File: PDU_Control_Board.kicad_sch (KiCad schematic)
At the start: 151 parts, among them J1 24V, J10 Precharge_2, J11 Shunt_2, J12 VIN_Enable, J13 VDC_IN_P, J14 VDC_IN_N, J15 VDC_OUT1_P, J16 VDC_OUT1_N, J17 VDC_OUT2_P, J18 VDC_OUT2_N, J19 24V, J2 Shunt_1, J3 SWD, J4 Precharge_1, J5 Precharge_2, J6 Shunt_2, J7 VIN_Enable, J8 Precharge_1, J9 Shunt_1, Q1 BSP75N, Q2 BSP75N, Q3 BSP75N, Q4 BSP75N, Q5 BSP75N, U1 LMV321, U2 APM32F405xG, U3 LMV321, U4 LMV321, U5 LMV321, Y2 X322516MOB4SI

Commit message: VER1.0: добавил в схему индикацию замыкания
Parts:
- removed J10: Precharge_2, Connector_PinHeader_2.54mm:PinHeader_2x02_P2.54mm_Vertical, symbol Connector_Generic:Conn_02x02_Odd_Even
- removed J11: Shunt_2, Connector_PinHeader_2.54mm:PinHeader_2x02_P2.54mm_Vertical, symbol Connector_Generic:Conn_02x02_Odd_Even
- removed J12: VIN_Enable, Connector_PinHeader_2.54mm:PinHeader_2x02_P2.54mm_Vertical, symbol Connector_Generic:Conn_02x02_Odd_Even
- removed J13: VDC_IN_P, Connector_PinHeader_2.54mm:PinHeader_2x02_P2.54mm_Vertical, symbol Connector_Generic:Conn_02x02_Odd_Even
- removed J14: VDC_IN_N, Connector_PinHeader_2.54mm:PinHeader_2x02_P2.54mm_Vertical, symbol Connector_Generic:Conn_02x02_Odd_Even
- removed J15: VDC_OUT1_P, Connector_PinHeader_2.54mm:PinHeader_2x02_P2.54mm_Vertical, symbol Connector_Generic:Conn_02x02_Odd_Even
- removed J16: VDC_OUT1_N, Connector_PinHeader_2.54mm:PinHeader_2x02_P2.54mm_Vertical, symbol Connector_Generic:Conn_02x02_Odd_Even
- removed J17: VDC_OUT2_P, Connector_PinHeader_2.54mm:PinHeader_2x02_P2.54mm_Vertical, symbol Connector_Generic:Conn_02x02_Odd_Even
- removed J18: VDC_OUT2_N, Connector_PinHeader_2.54mm:PinHeader_2x02_P2.54mm_Vertical, symbol Connector_Generic:Conn_02x02_Odd_Even
- removed J19: 24V, Connector_PinHeader_2.54mm:PinHeader_2x02_P2.54mm_Vertical, symbol Connector_Generic:Conn_02x02_Odd_Even
- removed J8: Precharge_1, Connector_PinHeader_2.54mm:PinHeader_2x02_P2.54mm_Vertical, symbol Connector_Generic:Conn_02x02_Odd_Even
- removed J9: Shunt_1, Connector_PinHeader_2.54mm:PinHeader_2x02_P2.54mm_Vertical, symbol Connector_Generic:Conn_02x02_Odd_Even
- added C39, C40, C41, C42, C43: 2.2u, Capacitor_SMD:C_0805_2012Metric_Pad1.18x1.45mm_HandSolder, symbol Device:C_Small
- added J10: Precharge_2, Connector_Molex:Molex_Mini-Fit_Jr_5569-02A2_2x01_P4.20mm_Horizontal, symbol Connector_Generic:Conn_01x02
- added J11: Shunt_2, Connector_Molex:Molex_Mini-Fit_Jr_5569-02A2_2x01_P4.20mm_Horizontal, symbol Connector_Generic:Conn_01x02
- added J12: VIN_Enable, Connector_Molex:Molex_Mini-Fit_Jr_5569-02A2_2x01_P4.20mm_Horizontal, symbol Connector_Generic:Conn_01x02
- added J20: VDC_OUT2, Connector_Molex:Molex_Mini-Fit_Jr_5569-02A2_2x01_P4.20mm_Horizontal, symbol Connector_Generic:Conn_01x02
- added J21: VDC_OUT1, Connector_Molex:Molex_Mini-Fit_Jr_5569-02A2_2x01_P4.20mm_Horizontal, symbol Connector_Generic:Conn_01x02
- added J22: VDC_IN, Connector_Molex:Molex_Mini-Fit_Jr_5569-02A2_2x01_P4.20mm_Horizontal, symbol Connector_Generic:Conn_01x02
- added J8: Precharge_1, Connector_Molex:Molex_Mini-Fit_Jr_5569-02A2_2x01_P4.20mm_Horizontal, symbol Connector_Generic:Conn_01x02
- added J9: Shunt_1, Connector_Molex:Molex_Mini-Fit_Jr_5569-02A2_2x01_P4.20mm_Horizontal, symbol Connector_Generic:Conn_01x02
- added Q10, Q6, Q7, Q8, Q9: BC817, Package_TO_SOT_SMD:SOT-23, symbol Transistor_BJT:BC817
- added R65, R67, R69, R71, R73: 2.2k, Resistor_SMD:R_0805_2012Metric_Pad1.20x1.40mm_HandSolder, symbol Device:R_Small
- added R66, R68, R70, R72, R74: 1k, Resistor_SMD:R_0805_2012Metric_Pad1.20x1.40mm_HandSolder, symbol Device:R_Small
- C14, C15: footprint Capacitor_SMD:C_0603_1608Metric_Pad1.08x0.95mm_HandSolder -> Capacitor_SMD:C_0805_2012Metric_Pad1.18x1.45mm_HandSolder
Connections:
- net +24V: now also J10.1 (Pin_1), J11.1 (Pin_1), J12.1 (Pin_1), J8.1 (Pin_1), J9.1 (Pin_1)
- net +3.3V: now also R66.2, R68.2, R70.2, R72.2, R74.2
- net GND: now also C39.2, C40.2, C41.2, C42.2, C43.2, Q10.2 (E), Q6.2 (E), Q7.2 (E), Q8.2 (E), Q9.2 (E)
- net VDC_IN_N: now also J22.2 (Pin_2)
- net VDC_IN_P: now also J22.1 (Pin_1)
- net VDC_IN_SENSE: now also U2.30 (PA5)
- net VDC_OUT1_N: now also J21.2 (Pin_2)
- net VDC_OUT1_P: now also J21.1 (Pin_1)
- net VDC_OUT1_SENSE: now also U2.31 (PA6)
- net VDC_OUT2_N: now also J20.2 (Pin_2)
- net VDC_OUT2_P: now also J20.1 (Pin_1)
- net VDC_OUT2_SENSE: now also U2.32 (PA7)
- new net: Q9.1 (B), R71.2
- new net: J12.2 (Pin_2), R73.1
- new net: Q10.1 (B), R73.2
- new net: J10.2 (Pin_2), R69.1
- new net: Q6.1 (B), R65.2
- new net: J9.2 (Pin_2), R67.1
- new net: Q7.1 (B), R67.2
- new net: J8.2 (Pin_2), R65.1
- new net: J11.2 (Pin_2), R71.1
- new net: Q8.1 (B), R69.2
- new net ~{Precharge_1_ON}: C39.1, Q6.3 (C), R66.1
- new net ~{Precharge_2_ON}: C41.1, Q8.3 (C), R70.1
- new net ~{Shunt_1_ON}: C40.1, Q7.3 (C), R68.1
- new net ~{Shunt_2_ON}: C42.1, Q9.3 (C), R72.1
- new net ~{VIN_Enable_ON}: C43.1, Q10.3 (C), R74.1
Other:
- note added: "Индикация замыкания контакторов"
- moved on the sheet: C13, C14, C15, C9, D10, D11, D12, D13, D14, D15, D3, D4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

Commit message: VER1.0: разместил все на плате
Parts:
- removed J1: 24V, Connector_Molex:Molex_Mini-Fit_Jr_5569-02A2_2x01_P4.20mm_Horizontal, symbol Connector_Generic:Conn_01x02
- added C44: 100n, Capacitor_SMD:C_0805_2012Metric_Pad1.18x1.45mm_HandSolder, symbol Device:C
- added C45: 0.27u, Capacitor_SMD:C_0805_2012Metric_Pad1.18x1.45mm_HandSolder, symbol Device:C
- added C46: 56p, Capacitor_SMD:C_0805_2012Metric_Pad1.18x1.45mm_HandSolder, symbol Device:C
- added D19, D20, D21, D22, D23, D24, D25, D26, D27: LED_Small, LED_SMD:LED_0805_2012Metric, symbol Device:LED_Small
- added D28: BAT54S, Package_TO_SOT_SMD:SOT-23, symbol Device:D_Dual_Series_AKC_Parallel
- added J1: Current_Sensor, Connector_Molex:Molex_Mini-Fit_Jr_5569-04A2_2x02_P4.20mm_Horizontal, symbol Connector_Generic:Conn_02x02_Odd_Even
- added J13: 1-776087-1, Connector_My:TE_1-776087-1, symbol Connector_My:1-776087-1
- added R75: 750, Resistor_SMD:R_0805_2012Metric_Pad1.20x1.40mm_HandSolder, symbol Device:R_Small
- added R76, R77, R78, R79, R80: 5.1k, Resistor_SMD:R_0805_2012Metric_Pad1.20x1.40mm_HandSolder, symbol Device:R_Small
- added R81, R82, R83: 100k, Resistor_SMD:R_1206_3216Metric_Pad1.30x1.75mm_HandSolder, symbol Device:R_Small
- added R84: 49.9, Resistor_SMD:R_0805_2012Metric_Pad1.20x1.40mm_HandSolder, symbol Device:R
- added R85: 120, Resistor_SMD:R_0805_2012Metric_Pad1.20x1.40mm_HandSolder, symbol Device:R
- added U6: LMV321, Package_TO_SOT_SMD:SOT-23-5, symbol Amplifier_Operational:LMV321
- C22, C23, C29, C30, C31, C32, C34, C35, C36, C37, C38, C8: footprint Capacitor_SMD:C_0603_1608Metric -> Capacitor_SMD:C_0805_2012Metric_Pad1.18x1.45mm_HandSolder
- R14, R21, R22, R29, R30, R31, R38, R39, R46, R47, R48, R55, R56, R63, R64: footprint Resistor_SMD:R_0603_1608Metric -> Resistor_SMD:R_0805_2012Metric_Pad1.20x1.40mm_HandSolder
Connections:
- net +3.3V: now also C44.1, D19.2 (A), D28.2 (K), U6.5 (V+)
- net GND: now also C44.2, C45.2, C46.2, D28.1 (K), R75.2, R76.2, R77.2, R78.2, R79.2, R80.2, U6.2 (V-)
- net VDC_IN_N: now also D27.1 (K)
- net VDC_IN_P: now also R83.1
- net VDC_IN_SENSE: now also U2.33 (PC4); no longer U2.30 (PA5)
- net VDC_OUT1_N: now also D26.1 (K)
- net VDC_OUT1_P: now also R82.1
- net VDC_OUT1_SENSE: now also U2.32 (PA7); no longer U2.31 (PA6)
- net VDC_OUT2_N: now also D25.1 (K)
- net VDC_OUT2_P: now also R81.1
- net VDC_OUT2_SENSE: now also U2.31 (PA6); no longer U2.32 (PA7)
- net ~{Precharge_1_ON}: now also U2.67 (PA8)
- net ~{Precharge_2_ON}: now also U2.63 (PC6)
- net ~{Shunt_1_ON}: now also U2.65 (PC8)
- net ~{Shunt_2_ON}: now also U2.61 (PD14)
- net ~{VIN_Enable_ON}: now also U2.69 (PA10)
- net VIN_Enable: now reaches Q5.1 (G)
- net VIN_Enable: now also U2.68 (PA9)
- net Shunt_2: now reaches Q4.1 (G)
- net Shunt_2: now also U2.60 (PD13)
- net at J12.2 (Pin_2), R73.1: now also D20.2 (A)
- net at J10.2 (Pin_2), R69.1: now also D22.2 (A)
- net at J9.2 (Pin_2), R67.1: now also D23.2 (A)
- net at R49.2: no longer R50.1
- net Shunt_1: now reaches Q2.1 (G)
- net Shunt_1: now also U2.64 (PC7)
- net at J8.2 (Pin_2), R65.1: now also D24.2 (A)
- net at J11.2 (Pin_2), R71.1: now also D21.2 (A)
- net Precharge_1: now reaches Q1.1 (G)
- net Precharge_1: now also U2.66 (PC9)
- net Precharge_2: now reaches U2.62 (PD15)
- net Precharge_2: now also Q3.1 (G)
- net at R58.1: no longer R57.2
- new net: D21.1 (K), R77.1
- new net: D22.1 (K), R78.1
- new net: D20.1 (K), R76.1
- new net: D19.1 (K), R75.1
- new net: C46.1, R85.2, U6.1 (+)
- new net: D27.2 (A), R83.2
- new net: D25.2 (A), R81.2
- new net: D23.1 (K), R79.1
- new net: R84.1, U6.3 (-), U6.4
- new net: D26.2 (A), R82.2
- new net: D24.1 (K), R80.1
- new net Current: R85.1
- new net Current_SENSE: C45.1, D28.3 (A), R84.2, U2.30 (PA5)
- no-connect marks 56 -> 46
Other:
- note added: "Измерение тока"
- note removed: "Питание 24В"
- moved on the sheet: C14, C15, C24, C25, C26, C33, C35, C36, C37, C38, C39, C40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

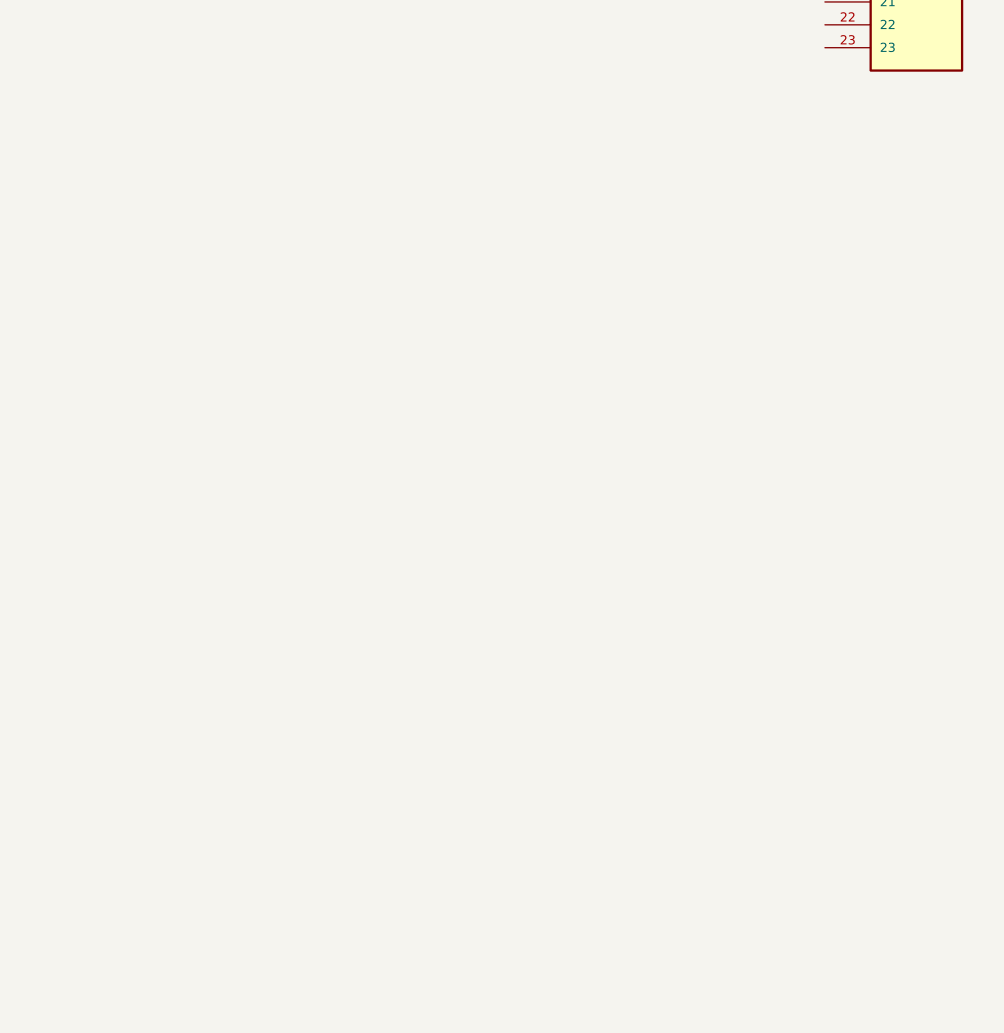
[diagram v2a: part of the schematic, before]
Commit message: VER1.0: добавил на плату все контакторы
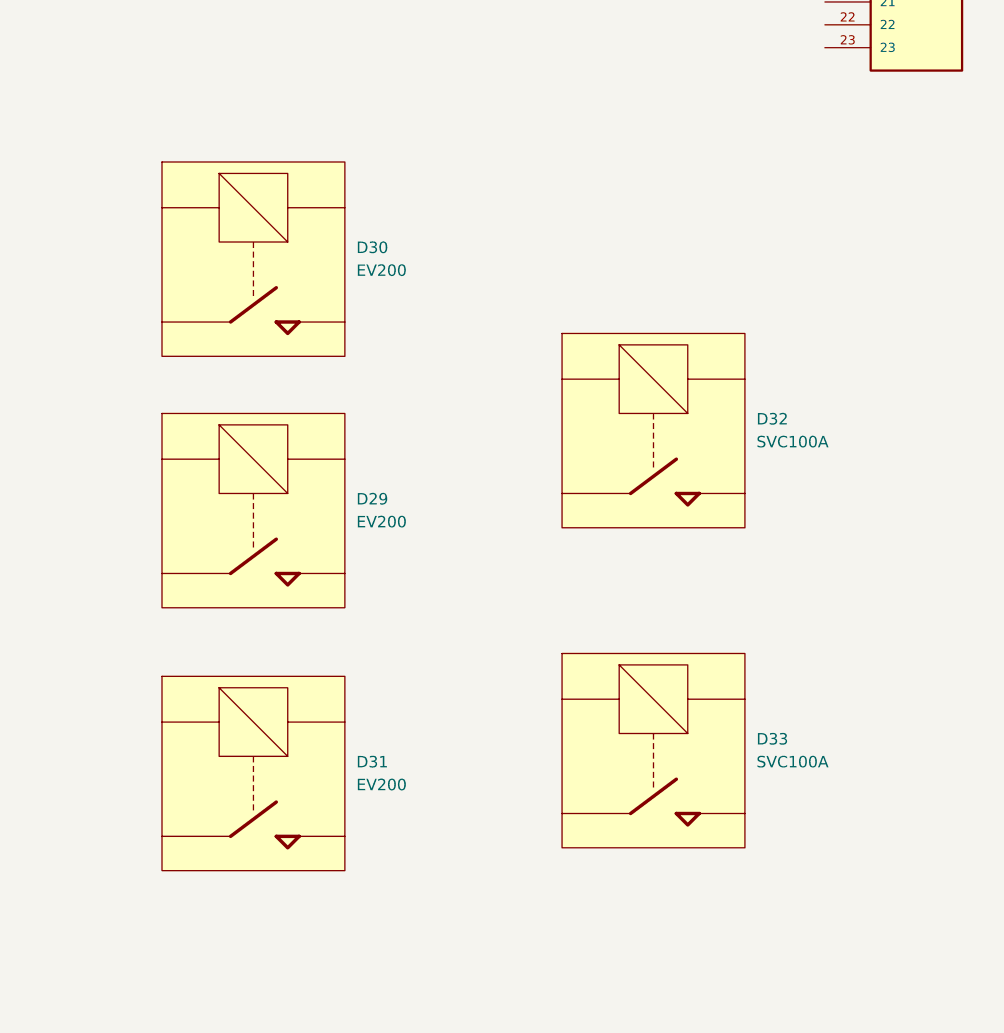
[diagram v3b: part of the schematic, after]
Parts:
- added D29, D30, D31: EV200, Contactor_My:EV200, symbol Contactor_My:EV200
- added D32, D33: SVC100A, Contactor_My:SVC100A, symbol Contactor_My:SVC100A
- J10, J11, J12, J2, J20, J21, J22, J4, J5, J6, J7, J8, J9: footprint Connector_Molex:Molex_Mini-Fit_Jr_5569-02A2_2x01_P4.20mm_Horizontal -> Connector_My:Mini-Fit_01x02_Vertical

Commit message: VER1.0: сделал отвязанное измерение напряжения
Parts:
- removed R33, R34, R35, R36, R37, R41, R42, R43, R44, R45, R49, R50, R51, R52, R53, R54, R57, R58, R59, R60, R61, R62: 249k, Resistor_SMD:R_1206_3216Metric, symbol Device:R
- removed R38, R46, R55, R63: 4.99k, Resistor_SMD:R_0805_2012Metric_Pad1.20x1.40mm_HandSolder, symbol Device:R
- added C47, C51, C54, C56, C59, C61: 0.1u, Capacitor_SMD:C_0805_2012Metric_Pad1.18x1.45mm_HandSolder, symbol Device:C
- added C48, C50, C53, C55, C58, C60: 2.2u, Capacitor_SMD:C_0805_2012Metric_Pad1.18x1.45mm_HandSolder, symbol Device:C
- added C49, C52, C57: 56p, Capacitor_SMD:C_0805_2012Metric_Pad1.18x1.45mm_HandSolder, symbol Device:C
- added C62: 1u, symbol Device:C_Polarized
- added C63: 10u, symbol Device:C_Polarized
- added C64: 100u, symbol Device:C_Polarized
- added D34, D35, D36: NSI1311, Package_SO:SOIC-8_7.5x5.85mm_P1.27mm, symbol NOVSENSE:NSI1311
- added D37: WRB2403S-3WR2, MORNSUN:WRB_S-3WR2, symbol MORNSUN:WRB_S-3WR2
- added D38, D39: LED_Small, LED_SMD:LED_0805_2012Metric, symbol Device:LED_Small
- added L1: L, symbol Device:L
- added R33, R34: 1k, Resistor_SMD:R_0805_2012Metric_Pad1.20x1.40mm_HandSolder, symbol Device:R_Small
- added R86: 120, Resistor_SMD:R_0805_2012Metric_Pad1.20x1.40mm_HandSolder, symbol Device:R
- added R87: 240, Resistor_SMD:R_1206_3216Metric, symbol Device:R
- added R88, R89: 47k, Resistor_SMD:R_1206_3216Metric, symbol Device:R
- C29, C30, C34, C35, C38, C8: value 4700p -> 56p
- J1: footprint Connector_Molex:Molex_Mini-Fit_Jr_5569-04A2_2x02_P4.20mm_Horizontal -> Connector_Molex:Molex_Mini-Fit_Jr_5566-04A_2x02_P4.20mm_Vertical
- R14, R30, R31, R47, R48, R64: value 3.74k -> 1k
- R15, R16, R23, R24: value 249k -> 47k
- R17, R25: value 249k -> 120; footprint Resistor_SMD:R_1206_3216Metric -> Resistor_SMD:R_0805_2012Metric_Pad1.20x1.40mm_HandSolder
- R18, R27: value 249k -> 240
- R19, R20, R26, R28: value 249k -> 1k; footprint Resistor_SMD:R_1206_3216Metric -> Resistor_SMD:R_0805_2012Metric_Pad1.20x1.40mm_HandSolder
- R21, R29: value 4.99k -> 1k
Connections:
- net +24V: now also C63.1, L1.1
- net +3.3V: no longer C21.1, C22.1, C31.1, C36.1, C44.1, D17.2 (K), D18.2 (K), D28.2 (K), D5.2 (K), U1.5 (V+), U3.5 (V+), U4.5 (V+), U5.5 (V+), U6.5 (V+)
- net +3.3VA: now also C21.1, C22.1, C31.1, C36.1, C44.1, D17.2 (K), D18.2 (K), D28.2 (K), D5.2 (K), U1.5 (V+), U3.5 (V+), U4.5 (V+), U5.5 (V+), U6.5 (V+), C50.2, C51.1, C55.2, C56.1, C60.2, C61.1, D34.8 (VDD2), D35.8 (VDD2), D36.8 (VDD2)
- net GND: now also C62.2, C63.2, D37.1 (GND), D38.1 (K), D39.1 (K); no longer C21.2, C22.2, C23.2, C27.2, C28.2, C30.1, C31.2, C32.2, C35.1, C36.2, C37.2, C44.2, C45.2, C46.2, C8.1, D17.1 (K), D18.1 (K), D28.1 (K), D5.1 (K), R14.1, R31.1, R48.1, R9.2, U1.2 (V-), U3.2 (V-), U4.2 (V-), U6.2 (V-)
- net GNDA: now also C21.2, C22.2, C23.2, C27.2, C28.2, C30.1, C31.2, C32.2, C35.1, C36.2, C37.2, C44.2, C45.2, C46.2, C8.1, D17.1 (K), D18.1 (K), D28.1 (K), D5.1 (K), R14.1, R31.1, R48.1, R9.2, U1.2 (V-), U3.2 (V-), U4.2 (V-), U6.2 (V-), C50.1, C51.2, C55.1, C56.2, C60.1, C61.2, D34.5 (GND2), D35.5 (GND2), D36.5 (GND2)
- net VDC_IN_N: no longer D27.1 (K), R23.1
- net VDC_IN_P: no longer R15.1, R83.1
- net VDC_OUT1_N: no longer D26.1 (K), R40.1
- net VDC_OUT1_P: no longer R82.1
- net VDC_OUT2_N: no longer D25.1 (K)
- net VDC_OUT2_P: no longer R81.1
- net at C29.1, R30.1: now also R29.2, U1.3 (-); no longer R28.2, R29.1
- net at R25.2: now also R24.1, R27.2; no longer R26.1
- net at R26.2: now also C35.2, R48.2, U5.1 (+); no longer R27.1
- net at C30.2, R31.2: now also R19.2, U3.1 (+)
- net at C34.1, R47.1: now also R20.2, U3.3 (-)
- net at R21.2, U1.1 (+): now also C8.2, R14.2
- net at R16.1: now also R17.2, R18.2; no longer R15.2
- net at U5.3 (-): now also C38.1, R28.2, R64.1
- net at R28.1: now also D36.6 (OUTN); no longer R27.2
- net at R17.1: now also C52.1, D35.2 (VIN); no longer R16.2
- net GNDPWR: now reaches R18.1
- net GNDPWR: now also D25.1 (K), D26.1 (K), D27.1 (K), R27.1, C47.2, C48.1, C49.2, C52.2, C53.1, C54.2, C57.2, C58.1, C59.2, D34.3 (SHTDN), D34.4 (GND1), D35.3 (SHTDN), D35.4 (GND1), D36.3 (SHTDN), D36.4 (GND1), R87.1; no longer R17.2
- net VDC_OUT1: now reaches R23.2
- net VDC_OUT1: now also R15.2, R82.1; no longer R24.1
- net at R20.1: now also D35.6 (OUTN); no longer R19.2
- net at U2.39 (PE8): now also R33.1
- net at U2.40 (PE9): now also R34.1
- net at R19.1: now also D35.7 (OUTP); no longer R18.2
- net at R25.1: now also C57.1, D36.2 (VIN); no longer R24.2
- new net: D38.2 (A), R33.2
- new net: D34.6 (OUTN), R29.1
- new net: C62.1, D37.2 (Vin), L1.2
- new net: R86.2, R87.2, R88.1
- new net: R88.2, R89.1
- new net: C64.1, D37.6 (+Vo)
- new net: C64.2, D37.7 (0V)
- new net: D36.7 (OUTP), R26.1
- new net: D34.7 (OUTP), R21.1
- new net: R15.1, R16.2
- new net: D39.2 (A), R34.2
- new net: C49.1, D34.2 (VIN), R86.1
- new net: R23.1, R24.2
- new net +3.3VP: C47.1, C48.2, C53.2, C54.1, C58.2, C59.1, D34.1 (VDD1), D35.1 (VDD1), D36.1 (VDD1)
- new net VDC_IN: R83.1, R89.2
- new net VDC_OUT2: R81.1
- no-connect marks 46 -> 49
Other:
- note added: "Блок контакторов"
- moved on the sheet: C22, C23, C29, C30, C31, C32, C34, C35, C36, C37, C38, C39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
